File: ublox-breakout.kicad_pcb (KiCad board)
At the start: 4 copper layers, 36 x 25 mm, 26 parts, among them J1 Conn_01x08, J2 Conn_01x08, J3 Conn_Coaxial, J4 USB_B_Micro, U1 LK112M33TR, U2 UBLOX_NEO-M8T-0, U3 USBLC6-2SC6, U4 LK112M33TR

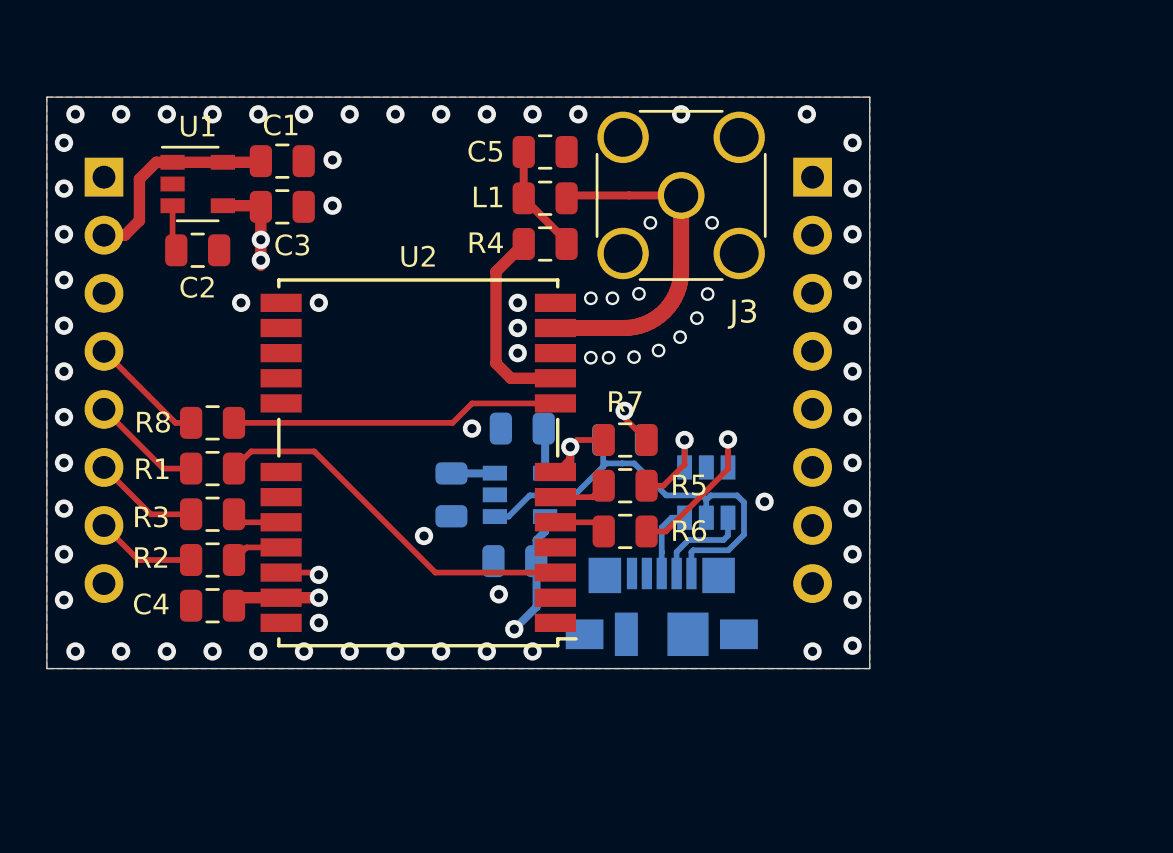
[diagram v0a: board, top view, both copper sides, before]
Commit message: Prototype LEA-M8 breakout board
includes fabrication Gerber files and BOM+CPL files for
JLCPCB SMT service.

PCB must be ordered with impedance control JLC7628 stack-up
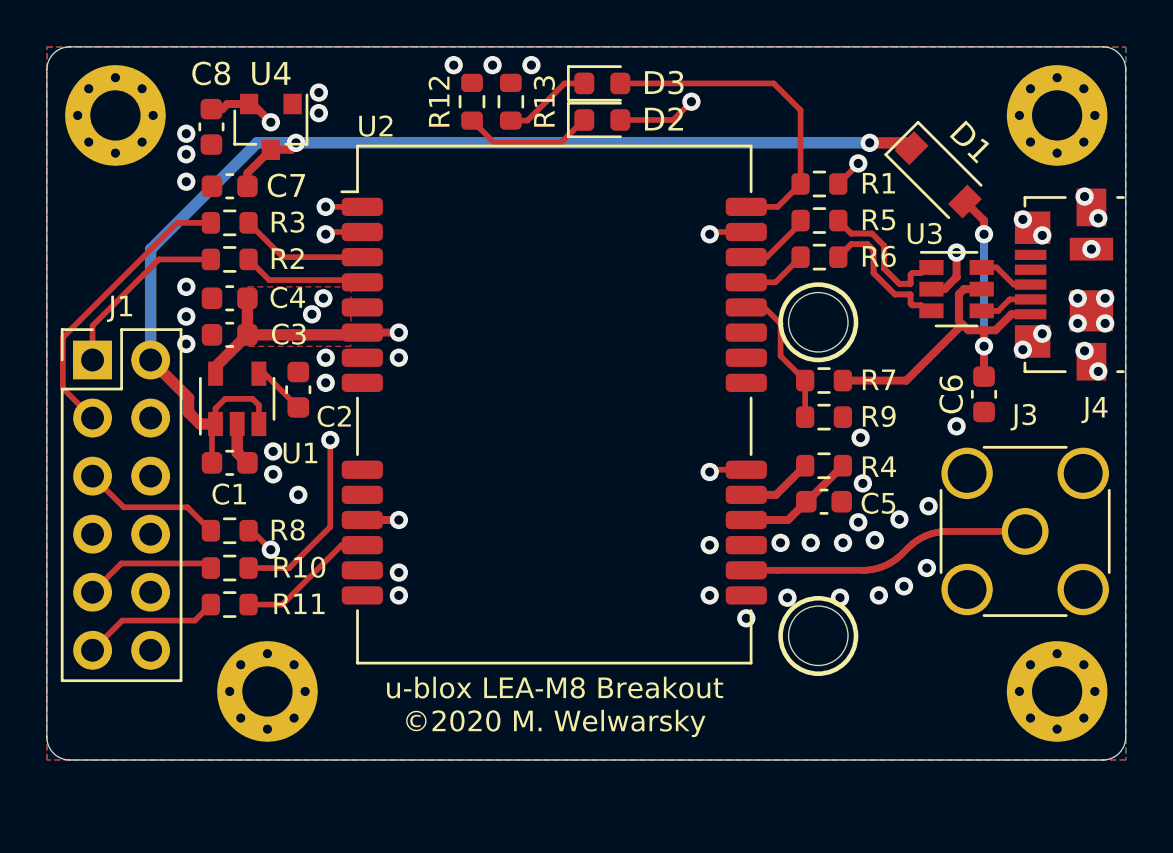
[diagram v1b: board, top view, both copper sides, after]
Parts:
- removed J2: Conn_01x08, Connector_PinSocket_2.54mm:PinSocket_1x08_P2.54mm_Vertical
- removed L1: 27nH, Inductor_SMD:L_0805_2012Metric
- added D1: B5819W, Diode_SMD:D_SOD-123, F.Cu at (158.5, 103.4)
- added D2: LED Green, LED_SMD:LED_0603_1608Metric, F.Cu at (143.8, 101.0)
- added D3: LED Red, LED_SMD:LED_0603_1608Metric, F.Cu at (143.8, 99.4)
- added H1: MountingHole_Pad, MountingHole:MountingHole_2.2mm_M2_Pad_Via, F.Cu at (122.5, 100.8)
- added H2: MountingHole_Pad, MountingHole:MountingHole_2.2mm_M2_Pad_Via, F.Cu at (163.7, 100.8)
- added H3: MountingHole_Pad, MountingHole:MountingHole_2.2mm_M2_Pad_Via, F.Cu at (163.7, 126.0)
- added H4: MountingHole_Pad, MountingHole:MountingHole_2.2mm_M2_Pad_Via, F.Cu at (129.2, 126.0)
- added R10: 27, Resistor_SMD:R_0603_1608Metric, F.Cu at (127.5, 120.6)
- added R11: 27, Resistor_SMD:R_0603_1608Metric, F.Cu at (127.5, 122.2)
- added R12: 620, Resistor_SMD:R_0603_1608Metric, F.Cu at (138.1, 100.2)
- added R13: 620, Resistor_SMD:R_0603_1608Metric, F.Cu at (139.8, 100.2)
- C1, C2, C3, C5: footprint Capacitor_SMD:C_0805_2012Metric -> Capacitor_SMD:C_0603_1608Metric
- C4: value 100n -> 1u; footprint Capacitor_SMD:C_0805_2012Metric -> Capacitor_SMD:C_0603_1608Metric
- C6: value 1u -> 100n; footprint Capacitor_SMD:C_0805_2012Metric -> Capacitor_SMD:C_0603_1608Metric; moved to F.Cu
- C7: value 100n -> 1u; footprint Capacitor_SMD:C_0805_2012Metric -> Capacitor_SMD:C_0603_1608Metric; moved to F.Cu
- C8: footprint Capacitor_SMD:C_0805_2012Metric -> Capacitor_SMD:C_0603_1608Metric; moved to F.Cu
- J1: value Conn_01x08 -> Conn_02x06_Odd_Even; footprint Connector_PinSocket_2.54mm:PinSocket_1x08_P2.54mm_Vertical -> Connector_PinHeader_2.54mm:PinHeader_2x06_P2.54mm_Vertical; moved to F.Cu
- J4, U3: moved to F.Cu
- R1, R2, R3, R8: value 22 -> 27; footprint Resistor_SMD:R_0805_2012Metric -> Resistor_SMD:R_0603_1608Metric
- R4, R5, R6: footprint Resistor_SMD:R_0805_2012Metric -> Resistor_SMD:R_0603_1608Metric
- R7: value 100k -> 62k; footprint Resistor_SMD:R_0805_2012Metric -> Resistor_SMD:R_0603_1608Metric
- R9: value 100k -> 110k; footprint Resistor_SMD:R_0805_2012Metric -> Resistor_SMD:R_0603_1608Metric; moved to F.Cu
- U1: value LK112M33TR -> ME6211C33M5G-N
- U2: value UBLOX_NEO-M8T-0 -> UBLOX_LEA-M8T-0; footprint project:UBLOX_NEO-M8T-0 -> RF_GPS:ublox_LEA
- U4: value LK112M33TR -> XC6206P332MR; footprint Package_TO_SOT_SMD:SOT-23-5 -> Package_TO_SOT_SMD:SOT-23; moved to F.Cu
- moved R1 29.3 mm to (153.3, 103.8)
- moved J4 22.6 mm to (164.0, 108.2), turned to 90 degrees
- moved C6 21.8 mm to (160.5, 113.0), turned to 270 degrees
- moved J3 21.0 mm to (162.3, 119.0)
- moved C5 19.6 mm to (153.5, 117.7)
- moved U4 19.4 mm to (129.3, 101.3), turned to 270 degrees
- moved C8 19.0 mm to (126.7, 101.3), turned to 270 degrees
- moved C7 16.6 mm to (127.5, 103.9), turned to 180 degrees
- moved R4 15.6 mm to (153.5, 116.1)
- moved R6 14.7 mm to (153.3, 107.0)
- moved R5 14.4 mm to (153.3, 105.4)
- moved U3 14.1 mm to (159.3, 108.4), turned to 0 degrees
- moved C4 13.5 mm to (127.5, 108.8)
- moved C1 13.4 mm to (127.5, 116.0)
- moved R2 13.2 mm to (127.5, 107.1)
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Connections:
- net /USB_DM renamed /USB_D-
- net /USB_DP renamed /USB_D+
- C6 pad 1: +5V -> /USB_VBUS
- C7 pad 1: Net-(C7-Pad1) -> +5V
- C8 pad 1: /VDD_USB -> VDD
- J1 pad 1: GND -> Net-(J1-Pad1)
- J1 pad 4: /GPS_RESET_N -> /SCL
- J1 pad 5: /GPS_1PPS -> Net-(J1-Pad5)
- J1 pad 6: /GPS_TXD -> /SDA
- J1 pad 7: /GPS_RXD -> (no net)
- J1 pad 8: GND -> (no net)
- J4 pad 4: Net-(J4-Pad4) -> (no net)
- R1 pad 1: /GPS_1PPS -> /TIMEPULSE
- R1 pad 2: Net-(R1-Pad2) -> Net-(J1-Pad10)
- R2 pad 1: /GPS_RXD -> Net-(J1-Pad1)
- R2 pad 2: Net-(R2-Pad2) -> /GPS_RXD
- R3 pad 1: /GPS_TXD -> Net-(J1-Pad3)
- R3 pad 2: Net-(R3-Pad2) -> /GPS_TXD
- R7 pad 2: GND -> /USB_VBUS
- R8 pad 1: Net-(R8-Pad1) -> Net-(J1-Pad5)
- R8 pad 2: /GPS_RESET_N -> /EXTINT1
- R9 pad 1: /USB_VBUS -> GND
- R9 pad 2: GND -> /VDD_USB
- U1 pad 3: Net-(C2-Pad1) -> +5V
- U1 pad 4: VDD -> Net-(C2-Pad1)
- U1 pad 5: +5V -> VDD
- U2 pad 1: Net-(U2-Pad1) -> /SDA
- U2 pad 10: GND -> (no net)
- U2 pad 11: /GPS_RF -> VDD
- U2 pad 12: GND -> /TIMEPULSE2
- U2 pad 14: Net-(U2-Pad14) -> GND
- U2 pad 15: Net-(U2-Pad15) -> GND
- U2 pad 16: Net-(U2-Pad16) -> /GPS_RF
- U2 pad 17: Net-(U2-Pad17) -> GND
- U2 pad 18: Net-(U2-Pad18) -> Net-(C5-Pad1)
- U2 pad 19: Net-(U2-Pad19) -> Net-(R4-Pad1)
- U2 pad 2: Net-(U2-Pad2) -> /SCL
- U2 pad 20: Net-(R3-Pad2) -> /EXTINT1
- U2 pad 21: Net-(R2-Pad2) -> (no net)
- U2 pad 22: VDD -> (no net)
- U2 pad 23: VDD -> (no net)
- U2 pad 24: GND -> /VDD_USB
- U2 pad 3: Net-(R1-Pad2) -> /GPS_TXD
- U2 pad 4: Net-(U2-Pad4) -> /GPS_RXD
- U2 pad 5: Net-(R6-Pad2) -> (no net)
- U2 pad 6: Net-(R5-Pad2) -> VDD
- U2 pad 7: /VDD_USB -> GND
- U2 pad 8: Net-(R8-Pad1) -> (no net)
- U2 pad 9: Net-(R4-Pad1) -> (no net)
- U4 pad 1: /USB_VBUS -> GND
- U4 pad 2: GND -> VDD
- U4 pad 3: Net-(C7-Pad1) -> +5V
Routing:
- net Net-(J1-Pad10): track 0.00 -> 42.1 mm, vias 0 -> 1
- net +5V: track 14.8 -> 53.3 mm, vias 1 -> 2
- net /EXTINT0: track 0.00 -> 30.1 mm, vias 0 -> 2
- net /EXTINT1: track 0.00 -> 23.6 mm, vias 0 -> 2
- net /SDA: track 0.00 -> 18.5 mm, vias 0 -> 1
- net Net-(R1-Pad2): track 16.7 -> 0.00 mm
- net Net-(R8-Pad1): track 14.5 -> 0.00 mm
- net /TIMEPULSE: track 0.00 -> 14.4 mm
- net /SCL: track 0.00 -> 13.6 mm, vias 0 -> 1
- net Net-(J1-Pad3): track 0.00 -> 12.6 mm
- net VDD: track 9.89 -> 18.6 mm, vias 4 -> 6
- net Net-(J1-Pad1): track 0.00 -> 7.88 mm
- net Net-(J1-Pad5): track 0.00 -> 6.16 mm
- net /TIMEPULSE2: track 0.00 -> 6.05 mm
- net Net-(J1-Pad11): track 0.00 -> 6.00 mm
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- added copper zone on F.Cu, net VDD
- removed copper zone on In2.Cu, net +5V
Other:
- board size 36 x 25 mm -> 47.2 x 31.2 mm
- net class 50Z added: clearance 0.5842, trace_width 0.29337, via_dia 0.8, via_drill 0.4
- net class USB added: clearance 0.2, trace_width 0.25, via_dia 0.8, via_drill 0.4
- rule pad_to_mask_clearance: 0.051 -> 0
- rule via_min_size: 0.4 -> 0.45
- board text added: "u-blox LEA-M8 Breakout ©2020 M. Welwarsky"

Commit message: Update LEA breakout board:
- add backup battery
- add buffered PPS output
- add pull-up resistors for SCL/SDA
- add D_SEL on pin header
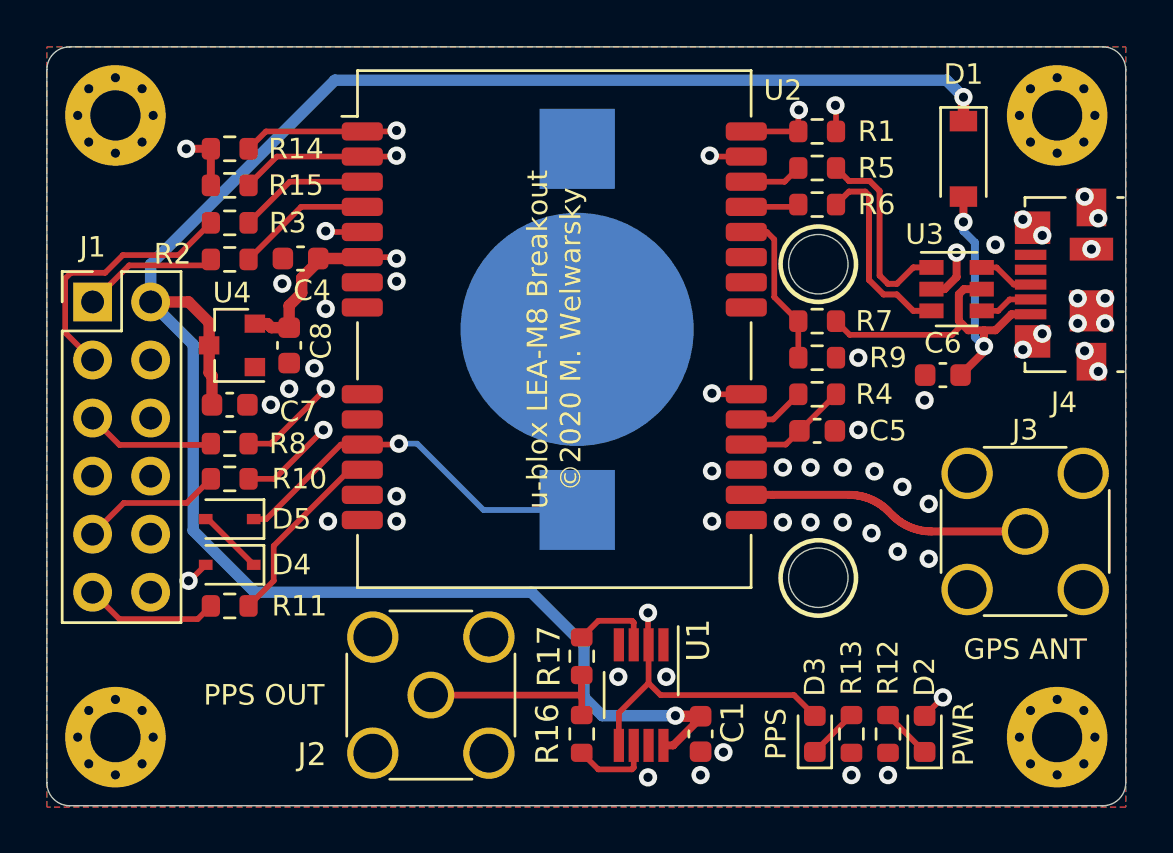
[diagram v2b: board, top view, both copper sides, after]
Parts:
- removed C2: 100n, Capacitor_SMD:C_0603_1608Metric
- removed C3: 1u, Capacitor_SMD:C_0603_1608Metric
- added BT1: Battery_Cell, Battery:BatteryHolder_Keystone_3000_1x12mm, B.Cu at (142.7, 110.2)
- added D4: 1N4148WS, Diode_SMD:D_SOD-323, F.Cu at (127.5, 120.5)
- added D5: 1N4148WS, Diode_SMD:D_SOD-323, F.Cu at (127.5, 118.5)
- added J2: Conn_Coaxial, Connector_Coaxial:SMA_Amphenol_132134_Vertical, F.Cu at (136.3, 126.2)
- added R14: 4k7, Resistor_SMD:R_0603_1608Metric, F.Cu at (127.5, 102.3)
- added R15: 4k7, Resistor_SMD:R_0603_1608Metric, F.Cu at (127.5, 103.9)
- added R16: 82, Resistor_SMD:R_0603_1608Metric, F.Cu at (142.9, 127.9)
- added R17: 82, Resistor_SMD:R_0603_1608Metric, F.Cu at (142.9, 124.5)
- C1: value 1u -> 100n
- U1: value ME6211C33M5G-N -> 74HCT2G125DP,125; footprint Package_TO_SOT_SMD:SOT-23-5 -> Package_SO:VSSOP-8_3.0x3.0mm_P0.65mm
- U3: value USBLC6-2SC6 -> TPUSBLC6-2SC6
- moved R12 33.1 mm to (156.3, 127.9), turned to 90 degrees
- moved R13 31.4 mm to (154.7, 127.9), turned to 90 degrees
- moved D2 30.3 mm to (157.9, 127.9), turned to 90 degrees
- moved D3 29.9 mm to (153.1, 127.9), turned to 90 degrees
- moved C1 23.8 mm to (148.1, 127.9), turned to 270 degrees
- moved U1 21.9 mm to (145.5, 126.2), turned to 270 degrees
- moved C8 10.1 mm to (130.1, 110.9)
- moved U4 9.71 mm to (127.6, 110.9), turned to 180 degrees
- moved C7 9.56 mm to (127.5, 113.5), turned to 0 degrees
- moved H4 6.94 mm to (122.5, 128.0)
- moved R10 3.90 mm to (127.5, 116.7)
- moved R8 3.81 mm to (127.5, 115.2)
- moved C4 3.55 mm to (130.6, 107.1)
- moved U2 3.30 mm to (141.7, 110.0)
- moved R4 3.14 mm to (153.2, 113.0)
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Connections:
- J1 pad 7: (no net) -> /D_SEL
- R10 pad 2: /EXTINT0 -> /EXTINT1
- R8 pad 2: /EXTINT1 -> /EXTINT0
- U1 pad 1: +5V -> GND
- U1 pad 2: GND -> /TIMEPULSE
- U1 pad 3: +5V -> Net-(R17-Pad2)
- U1 pad 4: Net-(C2-Pad1) -> GND
- U1 pad 5: VDD -> /TIMEPULSE
- U2 pad 11: VDD -> /V_BKP
- U2 pad 5: (no net) -> /D_SEL
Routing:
- net +5V: track 53.3 -> 88.9 mm
- net /TIMEPULSE: track 14.4 -> 42.2 mm, vias 0 -> 2
- net /D_SEL: track 0.00 -> 18.5 mm, vias 0 -> 1
- net /V_BKP: track 0.00 -> 18.0 mm, vias 0 -> 1
- net /SCL: track 13.6 -> 24.0 mm
- net /SDA: track 18.5 -> 27.8 mm
- net /PPS_OUT: track 0.00 -> 8.35 mm
- net VDD: track 18.6 -> 13.5 mm, vias 6 -> 4
- net Net-(J1-Pad10): track 42.1 -> 47.1 mm
- net Net-(R17-Pad2): track 0.00 -> 3.58 mm
- net Net-(R16-Pad2): track 0.00 -> 3.58 mm
- net Net-(D2-Pad1): track 5.71 -> 2.33 mm
- net /EXTINT0: track 30.1 -> 27.0 mm
- net Net-(D4-Pad1): track 0.00 -> 2.93 mm
- net /USB_D+: track 6.33 -> 8.74 mm
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- removed copper zone on F.Cu, net VDD
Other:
- board size 47.2 x 31.2 mm -> 47.2 x 33.2 mm
- board text added: "GPS ANT"
- board text added: "PPS"
- board text added: "PPS OUT"
- board text added: "PWR"

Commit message: BOM and schematic updates
- mark I2C pull-ups DNP (module has built-in pull resistors)
- small schematic cleanups
- add schematic PDF and board image
- update fabrication data
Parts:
- R14, R15: value 4k7 -> DNP
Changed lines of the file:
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@@
   (general
     (thickness 1.6)
-    (drawings 19)
+    (drawings 21)
     (tracks 328)
     (zones 0)
@@
     (pad_to_mask_clearance 0)
     (aux_axis_origin 119.5 131.06)
-    (grid_origin 121.5 108.96)
+    (grid_origin 119.5 131.01)
     (visible_elements FFFFFF7F)
     (pcbplotparams
@@
       (rotate (xyz 0 0 0))
     )
+    (model "${KIPRJMOD}/User Library-MCX_Plug_Straight.step"
+      (offset (xyz 11 -5 0))
+      (scale (xyz 1 1 1))
+      (rotate (xyz 0 0 0))
+    )
   )
   (module Resistor_SMD:R_0603_1608Metric (layer F.Cu)
@@
       (effects (font (size 0.9 0.9) (thickness 0.15)))
     )
-    (fp_text value 4k7 (at 0 1.43) (layer F.Fab)
+    (fp_text value DNP (at 0 1.43) (layer F.Fab)
       (effects (font (size 1 1) (thickness 0.15)))
     )
@@
     (pad 1 smd roundrect (at -0.825 0 180) (size 0.8 0.95) (layers F.Cu F.Paste F.Mask) (roundrect_rratio 0.25)
       (net 19 /SDA))
-    (model ${KISYS3DMOD}/Resistor_SMD.3dshapes/R_0603_1608Metric.wrl
-      (at (xyz 0 0 0))
-      (scale (xyz 1 1 1))
-      (rotate (xyz 0 0 0))
-    )
   )
   (module Diode_SMD:D_SOD-323 (layer F.Cu)
@@
       (effects (font (size 0.9 0.9) (thickness 0.15)))
     )
-    (fp_text value 4k7 (at 0 1.43) (layer F.Fab)
+    (fp_text value DNP (at 0 1.43) (layer F.Fab)
       (effects (font (size 1 1) (thickness 0.15)))
     )
@@
     (pad 1 smd roundrect (at -0.825 0 180) (size 0.8 0.95) (layers F.Cu F.Paste F.Mask) (roundrect_rratio 0.25)
       (net 21 /SCL))
-    (model ${KISYS3DMOD}/Resistor_SMD.3dshapes/R_0603_1608Metric.wrl
-      (at (xyz 0 0 0))
-      (scale (xyz 1 1 1))
-      (rotate (xyz 0 0 0))
-    )
   )
   (module Resistor_SMD:R_0603_1608Metric (layer F.Cu)
@@
     )
   )
+  (dimension 33.2 (width 0.15) (layer Dwgs.User)
+    (gr_text "33,200 mm" (at 117.4 114.4 270) (layer Dwgs.User)
+      (effects (font (size 1 1) (thickness 0.15)))
+    )
+    (feature1 (pts (xy 120.5 131) (xy 118.113579 131)))
+    (feature2 (pts (xy 120.5 97.8) (xy 118.113579 97.8)))
+    (crossbar (pts (xy 118.7 97.8) (xy 118.7 131)))
+    (arrow1a (pts (xy 118.7 131) (xy 118.113579 129.873496)))
+    (arrow1b (pts (xy 118.7 131) (xy 119.286421 129.873496)))
+    (arrow2a (pts (xy 118.7 97.8) (xy 118.113579 98.926504)))
+    (arrow2b (pts (xy 118.7 97.8) (xy 119.286421 98.926504)))
+  )
+  (dimension 47.2 (width 0.15) (layer Dwgs.User)
+    (gr_text "47,200 mm" (at 143.1 95.16) (layer Dwgs.User)
+      (effects (font (size 1 1) (thickness 0.15)))
+    )
+    (feature1 (pts (xy 166.7 98.8) (xy 166.7 95.873579)))
+    (feature2 (pts (xy 119.5 98.8) (xy 119.5 95.873579)))
+    (crossbar (pts (xy 119.5 96.46) (xy 166.7 96.46)))
+    (arrow1a (pts (xy 166.7 96.46) (xy 165.573496 97.046421)))
+    (arrow1b (pts (xy 166.7 96.46) (xy 165.573496 95.873579)))
+    (arrow2a (pts (xy 119.5 96.46) (xy 120.626504 97.046421)))
+    (arrow2b (pts (xy 119.5 96.46) (xy 120.626504 95.873579)))
+  )
   (gr_text "PPS OUT" (at 129 126.16) (layer F.SilkS)
